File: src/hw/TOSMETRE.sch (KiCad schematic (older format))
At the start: 54 parts, among them J1 Alim, J2 Conn_Coaxial, J3 Conn_01x08_Male, J5 Conn_Coaxial, SW1 SW_DIP_x01, SW2 SW_DIP_x01, SW3 SW_DIP_x01, U1 18F1320, U2 L7805, U3 LT1818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

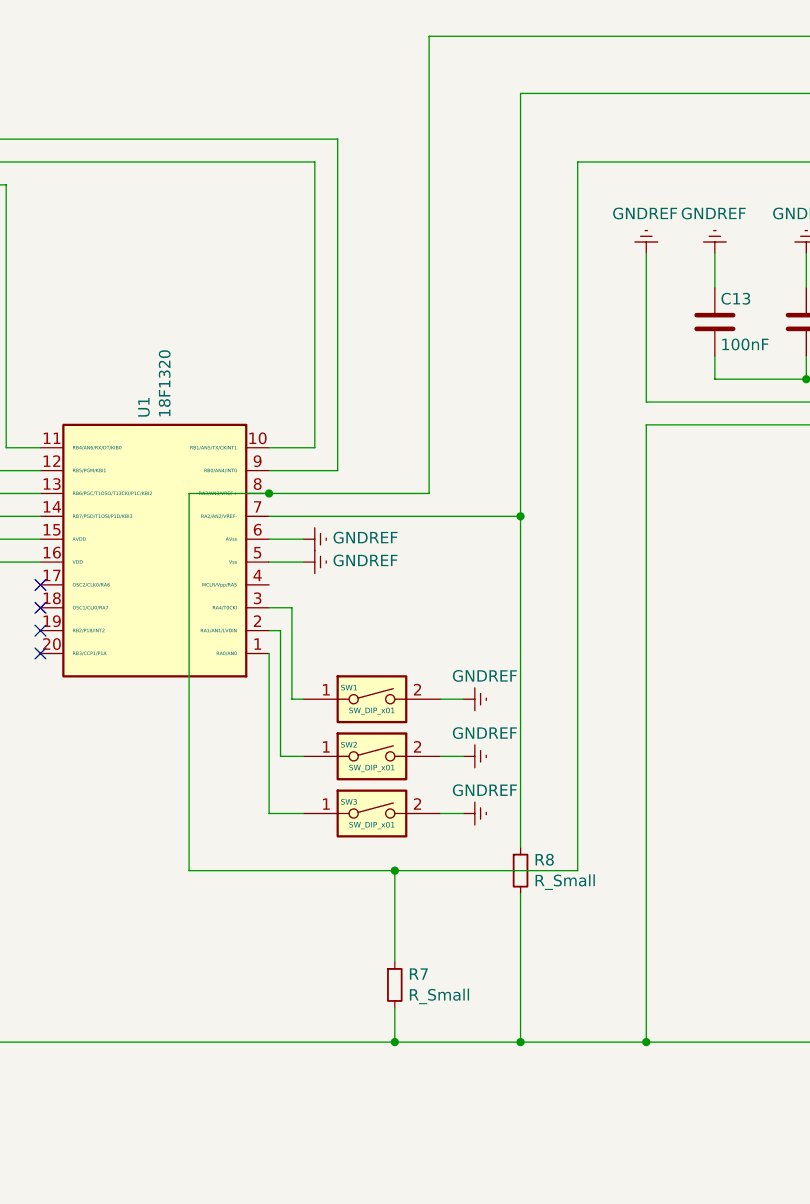
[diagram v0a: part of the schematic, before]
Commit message: modif bouton poussoir #307
modification bouton poussoir
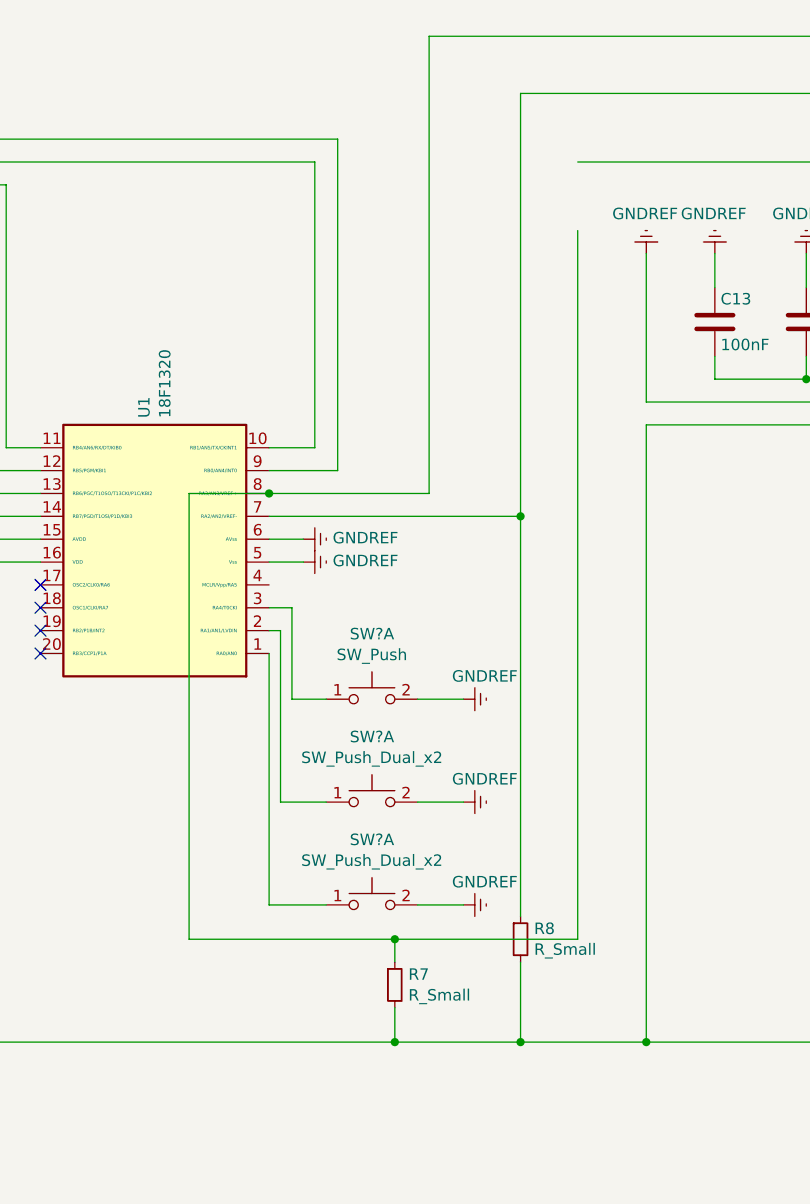
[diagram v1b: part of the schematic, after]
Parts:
- removed SW1, SW2, SW3: SW_DIP_x01, symbol Switch:SW_DIP_x01
- added SW?: SW_Push, symbol Switch:SW_Push_Dual_x2
- added SW? (x2): SW_Push_Dual_x2, symbol Switch:SW_Push_Dual_x2
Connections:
- net GNDREF: now also SW?.2 (D), SW?.2 (D), SW?.2 (D)
- net at U1.1 (RA0/AN0): now also SW?.1 (C)
- net at U1.2 (RA1/AN1/LVDIN): now also SW?.1 (C)
- net at U1.3 (RA4/T0CKI): now also SW?.1 (C)
- net at R7.1, U1.8 (RA3/AN3/VREF+), U4.8 (SDA): no longer U5.2 (SDA), U7.8 (SDA), U8.5 (SDA)
- new net: U5.2 (SDA), U7.8 (SDA), U8.5 (SDA)
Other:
- moved on the sheet: R8
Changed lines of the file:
@@
 L Device:R_Small R8
 U 1 1 5F3A76F9
-P 6500 7750
-F 0 "R8" H 6559 7796 50  0000 L CNN
-F 1 "R_Small" H 6559 7705 50  0000 L CNN
-F 2 "" H 6500 7750 50  0001 C CNN
-F 3 "~" H 6500 7750 50  0001 C CNN
-	1    6500 7750
+P 6500 8050
+F 0 "R8" H 6559 8096 50  0000 L CNN
+F 1 "R_Small" H 6559 8005 50  0000 L CNN
+F 2 "" H 6500 8050 50  0001 C CNN
+F 3 "~" H 6500 8050 50  0001 C CNN
+	1    6500 8050
 	1    0    0    -1
 $EndComp
@@
 	10650 6700 11400 6700
 Wire Wire Line
-	5950 8150 5950 7750
-Wire Wire Line
-	5950 8350 5950 8500
-Wire Wire Line
-	6500 7850 6500 8500
+	6500 8150 6500 8500
 Wire Wire Line
 	10900 4500 11100 4500
@@
 Wire Wire Line
 	5550 6300 5400 6300
-$Comp
-L Switch:SW_DIP_x01 SW1
-U 1 1 5F05F69E
-P 5850 7000
-F 0 "SW1" H 5750 7050 24  0000 C CNN
-F 1 "SW_DIP_x01" H 5850 6950 24  0000 C CNN
-F 2 "" H 5850 7000 50  0001 C CNN
-F 3 "~" H 5850 7000 50  0001 C CNN
-	1    5850 7000
-	1    0    0    -1
-$EndComp
 Wire Wire Line
 	6500 8500 7050 8500
@@
 Wire Wire Line
 	7050 5800 7050 8500
-$Comp
-L Switch:SW_DIP_x01 SW2
-U 1 1 5F0AD280
-P 5850 7250
-F 0 "SW2" H 5750 7300 24  0000 C CNN
-F 1 "SW_DIP_x01" H 5850 7200 24  0000 C CNN
-F 2 "" H 5850 7250 50  0001 C CNN
-F 3 "~" H 5850 7250 50  0001 C CNN
-	1    5850 7250
-	1    0    0    -1
-$EndComp
-$Comp
-L Switch:SW_DIP_x01 SW3
-U 1 1 5F0AE658
-P 5850 7500
-F 0 "SW3" H 5750 7550 24  0000 C CNN
-F 1 "SW_DIP_x01" H 5850 7450 24  0000 C CNN
-F 2 "" H 5850 7500 50  0001 C CNN
-F 3 "~" H 5850 7500 50  0001 C CNN
-	1    5850 7500
-	1    0    0    -1
-$EndComp
 Connection ~ 5950 8500
 Wire Wire Line
 	3700 8500 5950 8500
 Wire Wire Line
-	5050 7750 5950 7750
-Connection ~ 5950 7750
-Wire Wire Line
-	6500 6200 6500 7650
-Connection ~ 6500 6200
-Wire Wire Line
-	5950 7750 6750 7750
-Wire Wire Line
-	5050 6100 5050 7750
-Wire Wire Line
-	6750 4650 6750 7750
-Wire Wire Line
-	5400 7500 5400 6800
+	5050 8050 5950 8050
+Connection ~ 5950 8050
+Wire Wire Line
+	5950 8050 6750 8050
+Wire Wire Line
+	6750 4950 6750 8050
 Wire Wire Line
 	5400 6700 5450 6700
 Wire Wire Line
-	5450 6700 5450 7250
-Wire Wire Line
 	5400 6600 5500 6600
 Wire Wire Line
 	5500 6600 5500 7000
-Wire Wire Line
-	5500 7000 5550 7000
-Wire Wire Line
-	5450 7250 5550 7250
-Wire Wire Line
-	5550 7500 5400 7500
 $Comp
 L power:GNDREF #PWR?
@@
 L power:GNDREF #PWR?
 U 1 1 5F2B062F
-P 6250 7250
-F 0 "#PWR?" H 6250 7000 50  0001 C CNN
-F 1 "GNDREF" V 6350 7300 50  0000 R CNN
-F 2 "" H 6250 7250 50  0001 C CNN
-F 3 "" H 6250 7250 50  0001 C CNN
-	1    6250 7250
+P 6250 7450
+F 0 "#PWR?" H 6250 7200 50  0001 C CNN
+F 1 "GNDREF" V 6350 7500 50  0000 R CNN
+F 2 "" H 6250 7450 50  0001 C CNN
+F 3 "" H 6250 7450 50  0001 C CNN
+	1    6250 7450
 	0    -1   -1   0
 $EndComp
@@
 L power:GNDREF #PWR?
 U 1 1 5F2B0FD4
-P 6250 7500
-F 0 "#PWR?" H 6250 7250 50  0001 C CNN
-F 1 "GNDREF" V 6350 7550 50  0000 R CNN
-F 2 "" H 6250 7500 50  0001 C CNN
-F 3 "" H 6250 7500 50  0001 C CNN
-	1    6250 7500
-	0    -1   -1   0
-$EndComp
-Wire Wire Line
-	6250 7000 6150 7000
-Wire Wire Line
-	6250 7250 6150 7250
-Wire Wire Line
-	6250 7500 6150 7500
+P 6250 7900
+F 0 "#PWR?" H 6250 7650 50  0001 C CNN
+F 1 "GNDREF" V 6350 7950 50  0000 R CNN
+F 2 "" H 6250 7900 50  0001 C CNN
+F 3 "" H 6250 7900 50  0001 C CNN
+	1    6250 7900
+	0    -1   -1   0
+$EndComp
 Wire Wire Line
 	9750 5600 13600 5600
@@
 Text Notes 9250 710  0    60   ~ 0
 FWD\n
+$Comp
+L Switch:SW_Push_Dual_x2 SW?
+U 1 1 602CE788
+P 5850 7000
+F 0 "SW?" H 5850 7285 50  0000 C CNN
+F 1 "SW_Push" H 5850 7194 50  0000 C CNN
+F 2 "" H 5850 7200 50  0001 C CNN
+F 3 "~" H 5850 7200 50  0001 C CNN
+	1    5850 7000
+	1    0    0    -1
+$EndComp
+$Comp
+L Switch:SW_Push_Dual_x2 SW?
+U 1 1 602F02F4
+P 5850 7450
+F 0 "SW?" H 5850 7735 50  0000 C CNN
+F 1 "SW_Push_Dual_x2" H 5850 7644 50  0000 C CNN
+F 2 "" H 5850 7650 50  0001 C CNN
+F 3 "~" H 5850 7650 50  0001 C CNN
+	1    5850 7450
+	1    0    0    -1
+$EndComp
+$Comp
+L Switch:SW_Push_Dual_x2 SW?
+U 1 1 602F1015
+P 5850 7900
+F 0 "SW?" H 5850 8185 50  0000 C CNN
+F 1 "SW_Push_Dual_x2" H 5850 8094 50  0000 C CNN
+F 2 "" H 5850 8100 50  0001 C CNN
+F 3 "~" H 5850 8100 50  0001 C CNN
+	1    5850 7900
+	1    0    0    -1
+$EndComp
+Wire Wire Line
+	5500 7000 5650 7000
+Wire Wire Line
+	5450 7450 5650 7450
+Wire Wire Line
+	5400 7900 5650 7900
+Wire Wire Line
+	6050 7900 6250 7900
+Wire Wire Line
+	6050 7450 6250 7450
+Wire Wire Line
+	6050 7000 6250 7000
+Wire Wire Line
+	5950 8150 5950 8050
+Wire Wire Line
+	5950 8350 5950 8500
+Wire Wire Line
+	5050 6100 5050 8050
+Wire Wire Line
+	6500 6200 6500 7950
+Connection ~ 6500 6200
+Wire Wire Line
+	5400 6800 5400 7900
+Wire Wire Line
+	5450 6700 5450 7450
 $EndSCHEMATC
